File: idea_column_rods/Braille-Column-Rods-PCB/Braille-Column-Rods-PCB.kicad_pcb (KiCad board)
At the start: 2 copper layers, 76 x 95 mm, 64 parts, among them J1 Conn_01x06, J10 Screw_Terminal_01x02, J2 Conn_01x06, J3 Conn_01x06, J4 Conn_01x06, J9 Conn_01x02, M1 Stepper_Motor_bipolar, M2 Stepper_Motor_bipolar, M3 Stepper_Motor_bipolar, M4 Stepper_Motor_bipolar, SW1 SW_Push, SW2 SW_Push, U1 DRV8847SPWR, U2 DRV8847SPWR, U3 DRV8847SPWR, U4 DRV8847SPWR, U9 RP2040-Zero

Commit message: WIP: Rods PCB placement
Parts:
- removed H10, H11, H12, H9: MountingHole_Pad, 00-lib-footprints:MountingHole_2.2mm_M2_Pad_NoSilk
- removed H13, H14, H15, H16: MountingHole_Pad, 00-lib-footprints:MountingHole_3.2mm_M3_Pad_NoSilk
- removed H17, H18, H19, H20: MountingHole_Pad, 00-lib-footprints:HorizMounting_4x_M2_and_M3_Middle
- removed J10: Screw_Terminal_01x02, TerminalBlock:TerminalBlock_bornier-2_P5.08mm
- removed J9: Conn_01x02, Connector_PinHeader_2.54mm:PinHeader_1x02_P2.54mm_Vertical
- added C10: 10u, Capacitor_SMD:C_1206_3216Metric_Pad1.33x1.80mm_HandSolder, F.Cu at (129.5, 103.2)
- added C11: 10u, Capacitor_SMD:C_1206_3216Metric_Pad1.33x1.80mm_HandSolder, F.Cu at (170.1, 87.3)
- added C12: 10u, Capacitor_SMD:C_1206_3216Metric_Pad1.33x1.80mm_HandSolder, F.Cu at (301.4, 72.7)
- added C13: 10u, Capacitor_SMD:C_1206_3216Metric_Pad1.33x1.80mm_HandSolder, F.Cu at (159.7, 142.3)
- added C14: 100n, Capacitor_SMD:C_0603_1608Metric_Pad1.08x0.95mm_HandSolder, F.Cu at (305.0, 81.8)
- added C15: 100n, Capacitor_SMD:C_0603_1608Metric_Pad1.08x0.95mm_HandSolder, F.Cu at (305.0, 84.3)
- added C17: 100n, Capacitor_SMD:C_0603_1608Metric_Pad1.08x0.95mm_HandSolder, F.Cu at (274.8, 115.4)
- added C18: 100n, Capacitor_SMD:C_0603_1608Metric_Pad1.08x0.95mm_HandSolder, F.Cu at (274.8, 135.7)
- added C19: 100n, Capacitor_SMD:C_0603_1608Metric_Pad1.08x0.95mm_HandSolder, F.Cu at (290.4, 115.4)
- added C20: 100n, Capacitor_SMD:C_0603_1608Metric_Pad1.08x0.95mm_HandSolder, F.Cu at (259.1, 115.4)
- added C21: 100n, Capacitor_SMD:C_0603_1608Metric_Pad1.08x0.95mm_HandSolder, F.Cu at (306.1, 115.4)
- added C22: 100n, Capacitor_SMD:C_0603_1608Metric_Pad1.08x0.95mm_HandSolder, F.Cu at (311.4, 84.3)
- added C23: 100n, Capacitor_SMD:C_0603_1608Metric_Pad1.08x0.95mm_HandSolder, F.Cu at (290.4, 135.7)
- added C24: 100n, Capacitor_SMD:C_0603_1608Metric_Pad1.08x0.95mm_HandSolder, F.Cu at (259.1, 135.7)
- added C25: 4.7n, Capacitor_SMD:C_0603_1608Metric_Pad1.08x0.95mm_HandSolder, F.Cu at (274.8, 118.0)
- added C26: 4.7n, Capacitor_SMD:C_0603_1608Metric_Pad1.08x0.95mm_HandSolder, F.Cu at (274.8, 138.2)
- added C27: 4.7n, Capacitor_SMD:C_0603_1608Metric_Pad1.08x0.95mm_HandSolder, F.Cu at (290.4, 118.0)
- added C28: 4.7n, Capacitor_SMD:C_0603_1608Metric_Pad1.08x0.95mm_HandSolder, F.Cu at (259.1, 118.0)
- added C29: 4.7n, Capacitor_SMD:C_0603_1608Metric_Pad1.08x0.95mm_HandSolder, F.Cu at (306.1, 118.0)
- added C30: 4.7n, Capacitor_SMD:C_0603_1608Metric_Pad1.08x0.95mm_HandSolder, F.Cu at (311.4, 86.9)
- added C31: 4.7n, Capacitor_SMD:C_0603_1608Metric_Pad1.08x0.95mm_HandSolder, F.Cu at (290.4, 138.2)
- added C32: 4.7n, Capacitor_SMD:C_0603_1608Metric_Pad1.08x0.95mm_HandSolder, F.Cu at (259.1, 138.2)
- added C33: 100n, Capacitor_SMD:C_0603_1608Metric_Pad1.08x0.95mm_HandSolder, F.Cu at (93.5, 99.8)
- added C34: 4.7n, Capacitor_SMD:C_0603_1608Metric_Pad1.08x0.95mm_HandSolder, F.Cu at (93.5, 94.2)
- added C35: 100n, Capacitor_SMD:C_0603_1608Metric_Pad1.08x0.95mm_HandSolder, F.Cu at (175.2, 87.7)
- added C36: 4.7n, Capacitor_SMD:C_0603_1608Metric_Pad1.08x0.95mm_HandSolder, F.Cu at (175.2, 85.2)
- added C37: 100n, Capacitor_SMD:C_0603_1608Metric_Pad1.08x0.95mm_HandSolder, F.Cu at (296.2, 72.3)
- added C38: 4.7n, Capacitor_SMD:C_0603_1608Metric_Pad1.08x0.95mm_HandSolder, F.Cu at (296.2, 74.8)
- added C39: 100n, Capacitor_SMD:C_0603_1608Metric_Pad1.08x0.95mm_HandSolder, F.Cu at (164.9, 142.7)
- added C40: 4.7n, Capacitor_SMD:C_0603_1608Metric_Pad1.08x0.95mm_HandSolder, F.Cu at (164.9, 140.2)
- added C43: 100n, Capacitor_SMD:C_0603_1608Metric_Pad1.08x0.95mm_HandSolder, F.Cu at (305.0, 86.9)
- added C5: 100n, Capacitor_SMD:C_0603_1608Metric_Pad1.08x0.95mm_HandSolder, F.Cu at (306.1, 112.9)
- added C6: 100n, Capacitor_SMD:C_0603_1608Metric_Pad1.08x0.95mm_HandSolder, F.Cu at (311.4, 81.8)
- added C7: 100n, Capacitor_SMD:C_0603_1608Metric_Pad1.08x0.95mm_HandSolder, F.Cu at (290.4, 133.2)
- added C8: 100n, Capacitor_SMD:C_0603_1608Metric_Pad1.08x0.95mm_HandSolder, F.Cu at (259.1, 133.2)
- added D10: LED, LED_SMD:LED_0603_1608Metric_Pad1.05x0.95mm_HandSolder, F.Cu at (299.7, 146.9)
- added D11: LED, LED_SMD:LED_0603_1608Metric_Pad1.05x0.95mm_HandSolder, F.Cu at (268.4, 146.9)
- added D12: LED, LED_SMD:LED_0603_1608Metric_Pad1.05x0.95mm_HandSolder, F.Cu at (121.4, 105.2)
- added D13: LED, LED_SMD:LED_0603_1608Metric_Pad1.05x0.95mm_HandSolder, F.Cu at (164.8, 87.7)
- added D14: LED, LED_SMD:LED_0603_1608Metric_Pad1.05x0.95mm_HandSolder, F.Cu at (306.6, 72.3)
- added D15: LED, LED_SMD:LED_0603_1608Metric_Pad1.05x0.95mm_HandSolder, F.Cu at (160.5, 139.3)
- added D17: LED, LED_SMD:LED_0603_1608Metric_Pad1.05x0.95mm_HandSolder, F.Cu at (121.4, 107.0)
- added D18: LED, LED_SMD:LED_0603_1608Metric_Pad1.05x0.95mm_HandSolder, F.Cu at (164.8, 85.1)
- added D19: LED, LED_SMD:LED_0603_1608Metric_Pad1.05x0.95mm_HandSolder, F.Cu at (306.6, 74.9)
- added D20: LED, LED_SMD:LED_0603_1608Metric_Pad1.05x0.95mm_HandSolder, F.Cu at (160.5, 136.7)
- added D5: LED, LED_SMD:LED_0603_1608Metric_Pad1.05x0.95mm_HandSolder, F.Cu at (284.1, 146.9)
- added D6: LED, LED_SMD:LED_0603_1608Metric_Pad1.05x0.95mm_HandSolder, F.Cu at (299.7, 126.6)
- added D7: LED, LED_SMD:LED_0603_1608Metric_Pad1.05x0.95mm_HandSolder, F.Cu at (268.4, 126.6)
- added D8: LED, LED_SMD:LED_0603_1608Metric_Pad1.05x0.95mm_HandSolder, F.Cu at (315.4, 126.6)
- added D9: LED, LED_SMD:LED_0603_1608Metric_Pad1.05x0.95mm_HandSolder, F.Cu at (320.7, 95.5)
- added J5: Screw_Terminal_01x02, TerminalBlock:TerminalBlock_bornier-2_P5.08mm, F.Cu at (307.2, 136.5)
- added J6: Screw_Terminal_01x02, TerminalBlock:TerminalBlock_bornier-2_P5.08mm, F.Cu at (307.2, 145.5)
- added J7: Conn_01x02, Connector_PinHeader_2.54mm:PinHeader_1x02_P2.54mm_Vertical, F.Cu at (317.8, 144.0)
- added M10: Motor_DC_With_MP, 00-lib-footprints:DC_Motor_6mm_OD_with_3_Stage_Gearbox, F.Cu at (161.5, 97.0)
- added M11: Motor_DC_With_MP, 00-lib-footprints:DC_Motor_6mm_OD_with_3_Stage_Gearbox, F.Cu at (101.5, 152.0)
- added M12: Motor_DC_With_MP, 00-lib-footprints:DC_Motor_6mm_OD_with_3_Stage_Gearbox, F.Cu at (161.5, 152.0)
- added M5: Stepper_Motor_bipolar, 00-lib-footprints:MicroStepper_8mm-2mmGear, F.Cu at (313.1, 115.2)
- added M6: Stepper_Motor_bipolar, 00-lib-footprints:MicroStepper_8mm-2mmGear, F.Cu at (318.3, 84.1)
- added M7: Stepper_Motor_bipolar, 00-lib-footprints:MicroStepper_8mm-2mmGear, F.Cu at (297.4, 135.5)
- added M8: Stepper_Motor_bipolar, 00-lib-footprints:MicroStepper_8mm-2mmGear, F.Cu at (266.1, 135.5)
- added M9: Motor_DC_With_MP, 00-lib-footprints:DC_Motor_6mm_OD_with_3_Stage_Gearbox, F.Cu at (101.5, 97.0)
- added R13: 2k1, Resistor_SMD:R_0603_1608Metric_Pad0.98x0.95mm_HandSolder, F.Cu at (290.4, 123.0)
- added R14: 330m, Resistor_SMD:R_0603_1608Metric_Pad0.98x0.95mm_HandSolder, F.Cu at (290.4, 125.5)
- added R15: 330m, Resistor_SMD:R_0603_1608Metric_Pad0.98x0.95mm_HandSolder, F.Cu at (290.4, 128.0)
- added R16: 5k1, Resistor_SMD:R_0603_1608Metric_Pad0.98x0.95mm_HandSolder, F.Cu at (259.1, 120.5)
- added R23: 2k1, Resistor_SMD:R_0603_1608Metric_Pad0.98x0.95mm_HandSolder, F.Cu at (306.1, 123.0)
- added R24: 330m, Resistor_SMD:R_0603_1608Metric_Pad0.98x0.95mm_HandSolder, F.Cu at (306.1, 125.5)
- added R25: 330m, Resistor_SMD:R_0603_1608Metric_Pad0.98x0.95mm_HandSolder, F.Cu at (306.1, 128.0)
- added R26: 5k1, Resistor_SMD:R_0603_1608Metric_Pad0.98x0.95mm_HandSolder, F.Cu at (311.4, 89.4)
- added R31: 2k1, Resistor_SMD:R_0603_1608Metric_Pad0.98x0.95mm_HandSolder, F.Cu at (290.4, 143.2)
- added R32: 330m, Resistor_SMD:R_0603_1608Metric_Pad0.98x0.95mm_HandSolder, F.Cu at (290.4, 145.7)
- added R33: 330m, Resistor_SMD:R_0603_1608Metric_Pad0.98x0.95mm_HandSolder, F.Cu at (290.4, 148.2)
- added R34: 5k1, Resistor_SMD:R_0603_1608Metric_Pad0.98x0.95mm_HandSolder, F.Cu at (259.1, 140.7)
- added R35: 2k1, Resistor_SMD:R_0603_1608Metric_Pad0.98x0.95mm_HandSolder, F.Cu at (259.1, 143.2)
- added R36: 330m, Resistor_SMD:R_0603_1608Metric_Pad0.98x0.95mm_HandSolder, F.Cu at (259.1, 145.7)
- added R37: 330m, Resistor_SMD:R_0603_1608Metric_Pad0.98x0.95mm_HandSolder, F.Cu at (259.1, 148.2)
- added R38: 5k1, Resistor_SMD:R_0603_1608Metric_Pad0.98x0.95mm_HandSolder, F.Cu at (125.2, 105.9)
- added R39: 5k1, Resistor_SMD:R_0603_1608Metric_Pad0.98x0.95mm_HandSolder, F.Cu at (175.2, 82.7)
- added R40: 5k1, Resistor_SMD:R_0603_1608Metric_Pad0.98x0.95mm_HandSolder, F.Cu at (296.2, 77.3)
- added R41: 5k1, Resistor_SMD:R_0603_1608Metric_Pad0.98x0.95mm_HandSolder, F.Cu at (164.9, 137.7)
- added R43: 5k1, Resistor_SMD:R_0603_1608Metric_Pad0.98x0.95mm_HandSolder, F.Cu at (305.0, 89.4)
- added R5: 2k1, Resistor_SMD:R_0603_1608Metric_Pad0.98x0.95mm_HandSolder, F.Cu at (274.8, 123.0)
- added R6: 330m, Resistor_SMD:R_0603_1608Metric_Pad0.98x0.95mm_HandSolder, F.Cu at (274.8, 125.5)
- added R7: 330m, Resistor_SMD:R_0603_1608Metric_Pad0.98x0.95mm_HandSolder, F.Cu at (274.8, 128.0)
- added R8: 5k1, Resistor_SMD:R_0603_1608Metric_Pad0.98x0.95mm_HandSolder, F.Cu at (274.8, 140.7)
- added U10: AD116, Package_TO_SOT_SMD:SOT-23-6, F.Cu at (125.5, 103.0)
- added U11: AD116, Package_TO_SOT_SMD:SOT-23-6, F.Cu at (160.1, 86.6)
- added U12: AD116, Package_TO_SOT_SMD:SOT-23-6, F.Cu at (311.4, 73.5)
- added U13: AD116, Package_TO_SOT_SMD:SOT-23-6, F.Cu at (160.2, 133.0)
- added U14: 74HC595, Package_SO:SOP-16_3.9x9.9mm_P1.27mm, F.Cu at (294.2, 103.5)
- added U15: 74HC595, Package_SO:SOP-16_3.9x9.9mm_P1.27mm, F.Cu at (302.8, 103.5)
- added U17: MT910xET, Package_TO_SOT_SMD:SOT-23, F.Cu at (279.4, 127.7)
- added U18: MT910xET, Package_TO_SOT_SMD:SOT-23, F.Cu at (279.4, 148.0)
- added U19: MT910xET, Package_TO_SOT_SMD:SOT-23, F.Cu at (295.1, 127.7)
- added U20: MT910xET, Package_TO_SOT_SMD:SOT-23, F.Cu at (263.8, 127.7)
- added U21: MT910xET, Package_TO_SOT_SMD:SOT-23, F.Cu at (310.7, 127.7)
- added U22: MT910xET, Package_TO_SOT_SMD:SOT-23, F.Cu at (316.0, 96.6)
- added U23: MT910xET, Package_TO_SOT_SMD:SOT-23, F.Cu at (295.1, 148.0)
- added U24: MT910xET, Package_TO_SOT_SMD:SOT-23, F.Cu at (263.8, 148.0)
- added U25: MT910xET, Package_TO_SOT_SMD:SOT-23, F.Cu at (93.8, 97.0)
- added U26: MT910xET, Package_TO_SOT_SMD:SOT-23, F.Cu at (155.1, 86.6)
- added U27: MT910xET, Package_TO_SOT_SMD:SOT-23, F.Cu at (316.4, 73.5)
- added U28: MT910xET, Package_TO_SOT_SMD:SOT-23, F.Cu at (154.3, 141.6)
- added U30: CD74HC4067M, Package_SO:SOIC-24W_7.5x15.4mm_P1.27mm, F.Cu at (296.4, 89.2)
- added U5: DRV8847SPWR, Package_SO:TSSOP-16_4.4x5mm_P0.65mm, F.Cu at (266.1, 122.0)
- added U6: DRV8847SPWR, Package_SO:TSSOP-16_4.4x5mm_P0.65mm, F.Cu at (313.0, 122.0)
- added U7: DRV8847SPWR, Package_SO:TSSOP-16_4.4x5mm_P0.65mm, F.Cu at (318.3, 90.9)
- added U8: DRV8847SPWR, Package_SO:TSSOP-16_4.4x5mm_P0.65mm, F.Cu at (297.4, 142.3)
- C1, C2, C3, C4: footprint Capacitor_SMD:C_1206_3216Metric_Pad1.33x1.80mm_HandSolder -> Capacitor_SMD:C_0603_1608Metric_Pad1.08x0.95mm_HandSolder; moved to F.Cu
- D1, D2, D3, D4: footprint LED_SMD:LED_1206_3216Metric_Pad1.42x1.75mm_HandSolder -> LED_SMD:LED_0603_1608Metric_Pad1.05x0.95mm_HandSolder
- H1, H2, H3, H4, H5, H6: footprint 00-lib-footprints:MountingHole_8mm_Rect_NoSilk -> 00-lib-footprints:MountingHole_3.2mm_M3_Pad_NoSilk
- H7, H8: footprint 00-lib-footprints:MountingHole_2.2mm_M2_Pad_NoSilk -> 00-lib-footprints:MountingHole_3.2mm_M3_Pad_NoSilk
- J1: value Conn_01x06 -> Conn_01x03; footprint 00-lib-footprints:Braille_Cell_Pogos_Solder_2.5mmIntra_6.6x10mmInter -> Connector_PinHeader_2.54mm:PinHeader_1x03_P2.54mm_Vertical
- J2, J3: value Conn_01x06 -> Conn_01x02; footprint 00-lib-footprints:Braille_Cell_Pogos_Solder_2.5mmIntra_6.6x10mmInter -> Connector_PinHeader_2.54mm:PinHeader_1x02_P2.54mm_Vertical
- J4: value Conn_01x06 -> Conn_01x08; footprint 00-lib-footprints:Braille_Cell_Pogos_Solder_2.5mmIntra_6.6x10mmInter -> 00-lib-footprints:SOICbite_clipProgSmall
- R1, R17, R18, R2, R3, R4: footprint Resistor_SMD:R_1206_3216Metric_Pad1.30x1.75mm_HandSolder -> Resistor_SMD:R_0603_1608Metric_Pad0.98x0.95mm_HandSolder
- R10, R11: value 2k1 -> 330m; footprint Resistor_SMD:R_1206_3216Metric_Pad1.30x1.75mm_HandSolder -> Resistor_SMD:R_0603_1608Metric_Pad0.98x0.95mm_HandSolder; moved to F.Cu
- R12: value 2k1 -> 5k1; footprint Resistor_SMD:R_1206_3216Metric_Pad1.30x1.75mm_HandSolder -> Resistor_SMD:R_0603_1608Metric_Pad0.98x0.95mm_HandSolder; moved to F.Cu
- R19, R27: value 330m -> 2k1; footprint Resistor_SMD:R_1206_3216Metric_Pad1.30x1.75mm_HandSolder -> Resistor_SMD:R_0603_1608Metric_Pad0.98x0.95mm_HandSolder; moved to F.Cu
- R20, R21, R28, R29, R9: footprint Resistor_SMD:R_1206_3216Metric_Pad1.30x1.75mm_HandSolder -> Resistor_SMD:R_0603_1608Metric_Pad0.98x0.95mm_HandSolder; moved to F.Cu
- R22, R30: value 330m -> 5k1; footprint Resistor_SMD:R_1206_3216Metric_Pad1.30x1.75mm_HandSolder -> Resistor_SMD:R_0603_1608Metric_Pad0.98x0.95mm_HandSolder; moved to F.Cu
- SW1, SW2: footprint Button_Switch_THT:SW_PUSH_6mm -> 00-lib-footprints:PushButtonSMD_2.93x3.9
- U3: value DRV8847SPWR -> RP2040-Zero; footprint Package_SO:TSSOP-16_4.4x5mm_P0.65mm -> 00-lib-footprints:RP2040 Zero
- U9: value RP2040-Zero -> DRV8847SPWR; footprint 00-lib-footprints:RP2040 Zero -> Package_SO:TSSOP-16_4.4x5mm_P0.65mm
- moved R27 224.0 mm to (311.4, 91.9), turned to 0 degrees
- moved J1 220.5 mm to (317.8, 134.3)
- moved R28 210.7 mm to (311.4, 94.4), turned to 0 degrees
- moved R29 209.7 mm to (311.4, 96.9), turned to 0 degrees
- moved M3 190.9 mm to (297.4, 115.2)
- moved D1 187.7 mm to (284.1, 126.6)
- moved R22 186.6 mm to (306.1, 120.5), turned to 0 degrees
- moved U1 185.1 mm to (281.7, 122.0)
- moved M1 185.1 mm to (281.8, 115.2)
- moved R2 183.2 mm to (285.2, 103.2)
- moved C3 182.1 mm to (290.4, 112.9), turned to 0 degrees
- moved R3 181.3 mm to (285.2, 105.7)
- moved R1 180.7 mm to (274.8, 120.5)
- moved J3 179.2 mm to (285.6, 93.0)
- moved C1 178.3 mm to (274.8, 112.9), turned to 0 degrees
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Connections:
- C1 pad 1: Vdrive -> VDC
- C2 pad 1: Vdrive -> VDC
- C3 pad 1: Vdrive -> VDC
- C4 pad 1: Vdrive -> VDC
- D1 pad 1: /Braille_Cell/~{FAULT} -> /Motor_Control/Braille_Cell_Column/~{FAULT}
- D2 pad 1: /Braille_Cell1/~{FAULT} -> GND
- D3 pad 1: /Braille_Cell2/~{FAULT} -> GND
- D4 pad 1: /Braille_Cell3/~{FAULT} -> GND
- J1 pad 1: unconnected-(J1-Pin_1-Pad1) -> +5V
- J1 pad 2: unconnected-(J1-Pin_2-Pad2) -> VDC
- J1 pad 3: unconnected-(J1-Pin_3-Pad3) -> +3V3
- J2 pad 1: unconnected-(J2-Pin_1-Pad1) -> Net-(J2-Pin_1)
- J2 pad 2: unconnected-(J2-Pin_2-Pad2) -> Net-(J2-Pin_2)
- J3 pad 1: unconnected-(J3-Pin_1-Pad1) -> /Microcontroller/UART0_TX
- J3 pad 2: unconnected-(J3-Pin_2-Pad2) -> /Microcontroller/UART0_RX
- J4 pad 2: unconnected-(J4-Pin_2-Pad2) -> /Microcontroller/UART0_RX
- J4 pad 3: unconnected-(J4-Pin_3-Pad3) -> /Microcontroller/UART0_TX
- J4 pad 4: unconnected-(J4-Pin_4-Pad4) -> GND
- M3 pad 1: Net-(U3-OUT1) -> Net-(U4-OUT1)
- M3 pad 3: Net-(U3-OUT3) -> Net-(U4-OUT3)
- M3 pad 4: Net-(U3-OUT4) -> Net-(U4-OUT4)
- M4 pad 1: Net-(U4-OUT1) -> Net-(U5-OUT1)
- M4 pad 3: Net-(U4-OUT3) -> Net-(U5-OUT3)
- M4 pad 4: Net-(U4-OUT4) -> Net-(U5-OUT4)
- R1 pad 2: /Braille_Cell/~{FAULT} -> /Motor_Control/Braille_Cell_Column/~{FAULT}
- R10 pad 1: +3V3 -> Net-(U2-ISEN34)
- R10 pad 2: Net-(D2-A) -> GND
- R11 pad 1: +3V3 -> Net-(U2-ISEN12)
- R11 pad 2: Net-(D3-A) -> GND
- R12 pad 2: Net-(D4-A) -> /Motor_Control/Braille_Cell_Column2/~{FAULT}
- R19 pad 1: Net-(U1-ISEN34) -> +3V3
- R19 pad 2: GND -> Net-(D7-A)
- R2 pad 1: +3V3 -> /Microcontroller/GP_LED_0
- R2 pad 2: /Braille_Cell1/~{FAULT} -> Net-(D2-A)
- R20 pad 1: Net-(U2-ISEN34) -> Net-(U5-ISEN34)
- R21 pad 1: Net-(U3-ISEN34) -> Net-(U5-ISEN12)
- R22 pad 1: Net-(U4-ISEN34) -> +3V3
- R22 pad 2: GND -> /Motor_Control/Braille_Cell_Column4/~{FAULT}
- R27 pad 1: Net-(U1-ISEN12) -> +3V3
- R27 pad 2: GND -> Net-(D9-A)
- R28 pad 1: Net-(U2-ISEN12) -> Net-(U7-ISEN34)
- R29 pad 1: Net-(U3-ISEN12) -> Net-(U7-ISEN12)
- R3 pad 1: +3V3 -> VDC
- R3 pad 2: /Braille_Cell2/~{FAULT} -> Net-(D3-A)
- R30 pad 1: Net-(U4-ISEN12) -> +3V3
- R30 pad 2: GND -> /Motor_Control/Braille_Cell_Column6/~{FAULT}
- R4 pad 1: +3V3 -> /Microcontroller/GP_LED_1
- R4 pad 2: /Braille_Cell3/~{FAULT} -> Net-(D4-A)
- R9 pad 2: Net-(D1-A) -> Net-(D5-A)
- SW1 pad 2: Net-(U9-GP28) -> /Microcontroller/SW_1
- SW2 pad 2: Net-(U9-GP29) -> /Microcontroller/SW_2
- U1 pad 1: /Braille_Cell/~{SLEEP} -> /Motor_Control/Braille_Cell_Column/~{SLEEP}
- U1 pad 10: /Braille_Cell/IN4 -> unconnected-(U1-IN4-Pad10)
- U1 pad 12: Vdrive -> VDC
- U1 pad 15: /Braille_Cell/IN2 -> unconnected-(U1-IN2-Pad15)
- U1 pad 16: /Braille_Cell/IN1 -> unconnected-(U1-IN1-Pad16)
- U1 pad 8: /Braille_Cell/~{FAULT} -> /Motor_Control/Braille_Cell_Column/~{FAULT}
- U1 pad 9: /Braille_Cell/IN3 -> unconnected-(U1-IN3-Pad9)
- U2 pad 1: /Braille_Cell1/~{SLEEP} -> /Motor_Control/Braille_Cell_Column1/~{SLEEP}
- U2 pad 10: /Braille_Cell1/IN4 -> unconnected-(U2-IN4-Pad10)
- U2 pad 12: Vdrive -> VDC
- U2 pad 15: /Braille_Cell1/IN2 -> unconnected-(U2-IN2-Pad15)
- U2 pad 16: /Braille_Cell1/IN1 -> unconnected-(U2-IN1-Pad16)
- U2 pad 8: /Braille_Cell1/~{FAULT} -> /Motor_Control/Braille_Cell_Column1/~{FAULT}
- U2 pad 9: /Braille_Cell1/IN3 -> unconnected-(U2-IN3-Pad9)
- U3 pad 1: /Braille_Cell2/~{SLEEP} -> +5V
- U3 pad 10: /Braille_Cell2/IN4 -> /Microcontroller/UART0_TX
- U3 pad 11: I2C_SCL -> /Microcontroller/UART0_RX
- U3 pad 12: Vdrive -> /Microcontroller/SHIFT_SER_IN
- U3 pad 13: GND -> /Microcontroller/SHIFT_SRCK
- U3 pad 14: I2C_SDA -> /Microcontroller/~{SHIFT_SRCLR}
- U3 pad 15: /Braille_Cell2/IN2 -> /Microcontroller/SHIFT_RCLK
- U3 pad 16: /Braille_Cell2/IN1 -> /Microcontroller/~{SHIFT_OE}
- U3 pad 2: Net-(U3-OUT1) -> GND
- U3 pad 3: Net-(U3-ISEN12) -> +3V3
- U3 pad 4: Net-(M3--) -> unconnected-(U3-GP29-Pad4)
- U3 pad 5: Net-(U3-OUT4) -> /Microcontroller/SW_1
- U3 pad 6: Net-(U3-ISEN34) -> /Microcontroller/SW_2
- U3 pad 7: Net-(U3-OUT3) -> /Microcontroller/HALL_ANALOG
- U3 pad 8: /Braille_Cell2/~{FAULT} -> Net-(J2-Pin_1)
- U3 pad 9: /Braille_Cell2/IN3 -> Net-(J2-Pin_2)
- U4 pad 1: /Braille_Cell3/~{SLEEP} -> /Motor_Control/Braille_Cell_Column2/~{SLEEP}
- U4 pad 10: /Braille_Cell3/IN4 -> unconnected-(U4-IN4-Pad10)
- U4 pad 12: Vdrive -> VDC
- U4 pad 15: /Braille_Cell3/IN2 -> unconnected-(U4-IN2-Pad15)
- U4 pad 16: /Braille_Cell3/IN1 -> unconnected-(U4-IN1-Pad16)
- U4 pad 4: Net-(M4--) -> Net-(M3--)
- U4 pad 8: /Braille_Cell3/~{FAULT} -> /Motor_Control/Braille_Cell_Column2/~{FAULT}
- U4 pad 9: /Braille_Cell3/IN3 -> unconnected-(U4-IN3-Pad9)
- U9 pad 1: +5V -> /Motor_Control/Braille_Cell_Column7/~{SLEEP}
- U9 pad 10: /Braille_Cell/~{FAULT} -> unconnected-(U9-IN4-Pad10)
- U9 pad 11: /Braille_Cell1/~{FAULT} -> I2C_SCL
- U9 pad 12: /Braille_Cell2/~{FAULT} -> VDC
- U9 pad 13: /Braille_Cell3/~{FAULT} -> GND
- U9 pad 14: /Braille_Cell/IN1 -> I2C_SDA
- U9 pad 15: /Braille_Cell/IN2 -> unconnected-(U9-IN2-Pad15)
- U9 pad 16: /Braille_Cell/IN3 -> unconnected-(U9-IN1-Pad16)
- U9 pad 2: GND -> Net-(U9-OUT1)
- U9 pad 3: +3V3 -> Net-(U9-ISEN12)
- U9 pad 4: Net-(U9-GP29) -> Net-(M8--)
- U9 pad 5: Net-(U9-GP28) -> Net-(U9-OUT4)
- U9 pad 6: I2C_SCL -> Net-(U9-ISEN34)
- U9 pad 7: I2C_SDA -> Net-(U9-OUT3)
- U9 pad 8: unconnected-(U9-GP15-Pad8)_1 -> /Motor_Control/Braille_Cell_Column7/~{FAULT}
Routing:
- net GND: track 192.0 -> 0.00 mm, vias 39 -> 0
- net Vdrive: track 166.6 -> 0.00 mm, vias 2 -> 0
- net I2C_SDA: track 150.7 -> 0.00 mm
- net I2C_SCL: track 148.8 -> 0.00 mm
- net +3V3: track 127.6 -> 1.91 mm, vias 3 -> 0
- net /Braille_Cell/~{FAULT}: track 83.4 -> 0.00 mm
- net /Braille_Cell1/~{FAULT}: track 61.6 -> 0.00 mm
- net /Braille_Cell2/~{FAULT}: track 58.1 -> 0.00 mm, vias 1 -> 0
- net /Braille_Cell2/~{SLEEP}: track 57.9 -> 0.00 mm, vias 1 -> 0
- net /Braille_Cell/IN1: track 51.7 -> 0.00 mm, vias 1 -> 0
- net /Braille_Cell/IN3: track 50.5 -> 0.00 mm, vias 1 -> 0
- net /Braille_Cell/IN2: track 50.4 -> 0.00 mm, vias 1 -> 0
- net /Braille_Cell/~{SLEEP}: track 48.4 -> 0.00 mm, vias 1 -> 0
- net /Braille_Cell/IN4: track 46.0 -> 0.00 mm, vias 1 -> 0
- net /Braille_Cell3/~{FAULT}: track 41.9 -> 0.00 mm, vias 1 -> 0
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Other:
- board size 76 x 95 mm -> 95 x 95 mm
- board text removed: "6.6mm Inter-Cell 2.5mm Intra-Cell M2, M3, and 8mm"
- board text removed: "Braille Display (Pogo + Solenoid) 2024-10-10"
- board text removed: "Vdr GND"
- board text removed: "Vdrive GND"

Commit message: WIP: Place the housing and motor X
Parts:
- removed H3, H4: MountingHole_Pad, 00-lib-footprints:MountingHole_3.2mm_M3_Pad_NoSilk
- H1, H2: footprint 00-lib-footprints:MountingHole_3.2mm_M3_Pad_NoSilk -> 00-lib-footprints:Braille_Block_MountingHoles_M2_3x
- moved U27 236.0 mm to (93.8, 152.1), turned to 180 degrees
- moved C37 218.8 mm to (93.5, 154.8), turned to 180 degrees
- moved C38 215.9 mm to (93.5, 149.2), turned to 180 degrees
- moved M6 209.1 mm to (115.8, 136.0), turned to 90 degrees
- moved U1 205.6 mm to (76.1, 125.3)
- moved U17 205.6 mm to (73.8, 131.0)
- moved C1 205.6 mm to (69.2, 116.2)
- moved C17 205.6 mm to (69.2, 118.7)
- moved C25 205.6 mm to (69.2, 121.2)
- moved R1 205.6 mm to (69.2, 123.7)
- moved R5 205.6 mm to (69.2, 126.2)
- moved R6 205.6 mm to (69.2, 128.7)
- moved R7 205.6 mm to (69.2, 131.2)
- moved D1 205.6 mm to (78.5, 129.9)
- moved D14 205.0 mm to (121.4, 160.2)
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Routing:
- net VDC: track 3.50 -> 14.0 mm
- net Net-(M12--): track 0.00 -> 9.26 mm
- net Net-(M11--): track 0.00 -> 9.26 mm
- net Net-(M10--): track 0.00 -> 9.26 mm
- net Net-(M12-+): track 0.00 -> 6.38 mm
- net Net-(M11-+): track 0.00 -> 6.38 mm
- net Net-(M10-+): track 0.00 -> 6.38 mm
- net +3V3: track 1.91 -> 7.64 mm
- net Net-(D15-A): track 0.00 -> 4.94 mm
- net Net-(D14-A): track 0.00 -> 4.94 mm
- net Net-(D13-A): track 0.00 -> 4.94 mm
- net /Motor_Control/Corner_DC_Motor3/IN_B: track 0.00 -> 4.30 mm
- net /Motor_Control/Corner_DC_Motor2/IN_B: track 0.00 -> 4.30 mm
- net /Motor_Control/Corner_DC_Motor1/IN_B: track 0.00 -> 4.30 mm
- net /Motor_Control/Corner_DC_Motor1/IN_A: track 0.00 -> 2.11 mm
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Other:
- board text added: "Cell Housing: * Mounting hole spacing (X) = 30.5mm * Center = (110.25mm, 125mm)"

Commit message: WIP: Position everything
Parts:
- C17, C25: moved to B.Cu
- M1, M2, M3, M4, M5, M6, M7, M8: footprint 00-lib-footprints:MicroStepper_8mm-2mmGear -> 00-lib-footprints:MicroStepper_4.7_OD
- moved C17 30.6 mm to (99.8, 116.4), turned to -90 degrees
- moved C25 28.9 mm to (97.8, 116.4), turned to -90 degrees
- moved U17 28.9 mm to (98.8, 116.3), turned to -90 degrees
- moved D20 5.03 mm to (141.8, 147.0)
- moved C10 5.00 mm to (129.5, 98.2)
- moved C11 5.00 mm to (133.5, 85.8)
- moved C12 5.00 mm to (129.5, 163.2)
- moved C13 5.00 mm to (133.5, 150.8)
- moved C33 5.00 mm to (93.5, 94.8)
- moved C34 5.00 mm to (93.5, 89.2)
- moved C35 5.00 mm to (169.5, 89.2)
- moved C36 5.00 mm to (169.5, 94.7)
- moved C37 5.00 mm to (93.5, 159.8)
- moved C38 5.00 mm to (93.5, 154.2)
- moved C39 5.00 mm to (169.5, 154.2)
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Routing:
- net /Motor_Control/Corner_DC_Motor/IN_B: track 4.30 -> 6.14 mm
- net /Motor_Control/HALL_0: vias 0 -> 1
- net +3V3: vias 0 -> 1

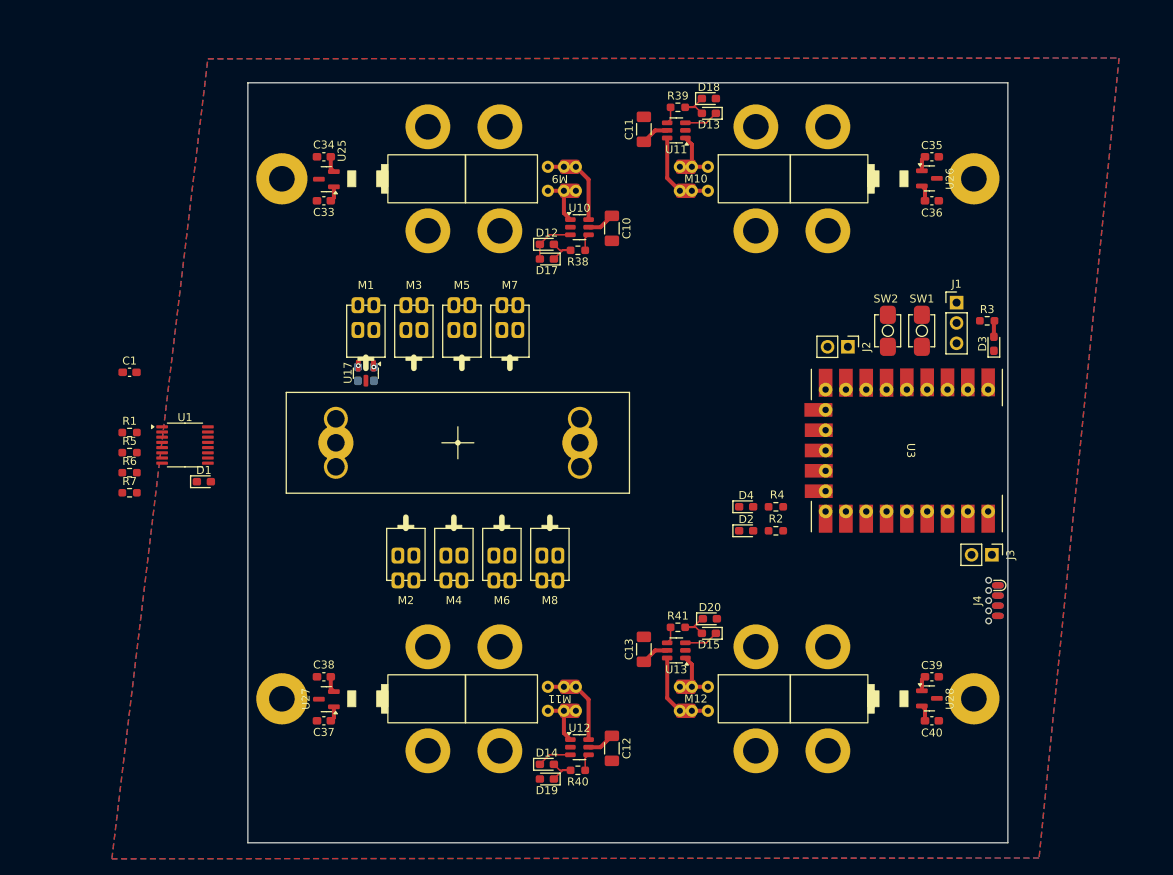
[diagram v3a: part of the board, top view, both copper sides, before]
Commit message: WIP: Update tight placement of DC motor
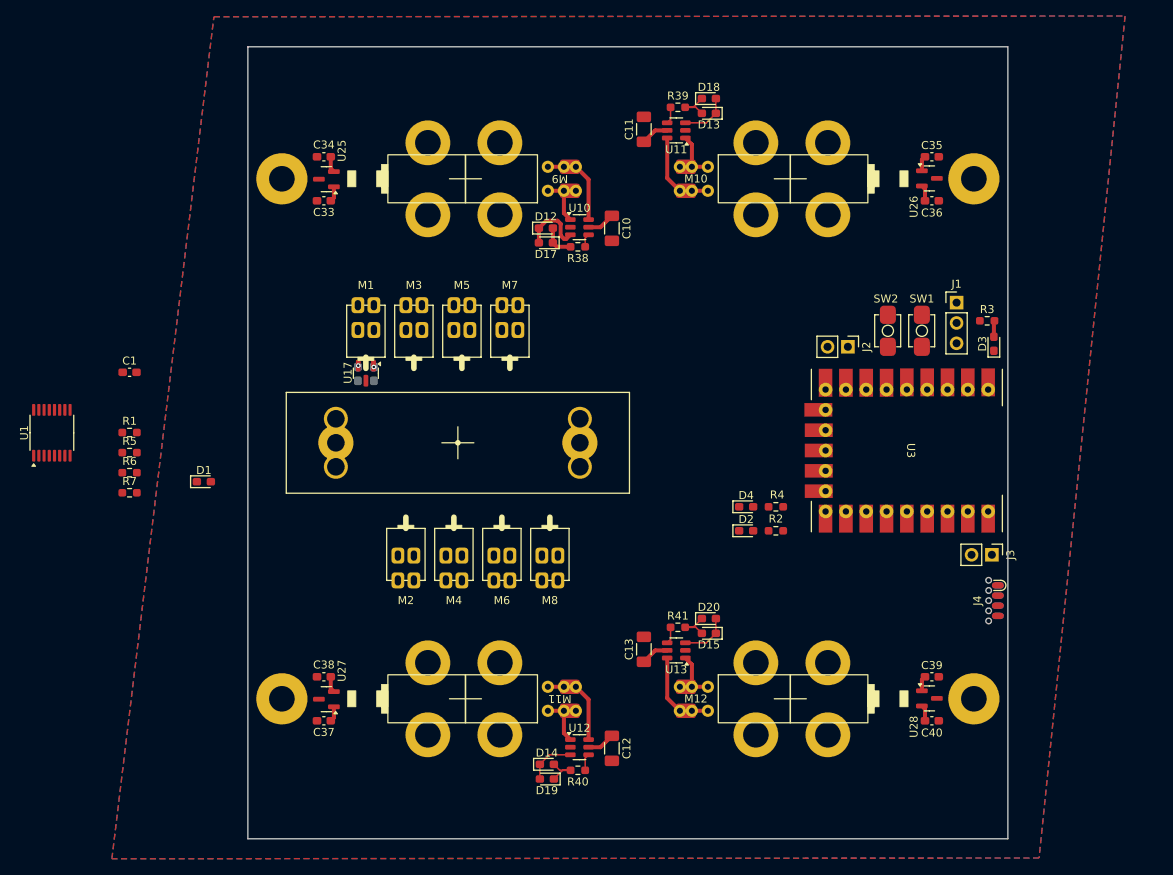
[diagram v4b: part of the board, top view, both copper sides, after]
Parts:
- moved U1 16.7 mm to (59.5, 123.8), turned to 90 degrees
- moved D12 2.03 mm to (121.2, 98.2)
- moved D17 2.03 mm to (121.2, 100.0)
- moved R38 0.44 mm to (125.2, 100.5)
- moved D20 0.13 mm to (141.6, 147.0)
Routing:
- net /Motor_Control/Corner_DC_Motor/IN_B: track 6.14 -> 8.17 mm
- net /Motor_Control/Corner_DC_Motor3/IN_B: track 4.30 -> 6.14 mm
- net /Motor_Control/Corner_DC_Motor2/IN_B: track 4.30 -> 6.14 mm
- net /Motor_Control/Corner_DC_Motor1/IN_B: track 4.30 -> 6.14 mm
- net Net-(D12-A): track 4.94 -> 4.26 mm
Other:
- board size 95 x 95 mm -> 95 x 99 mm

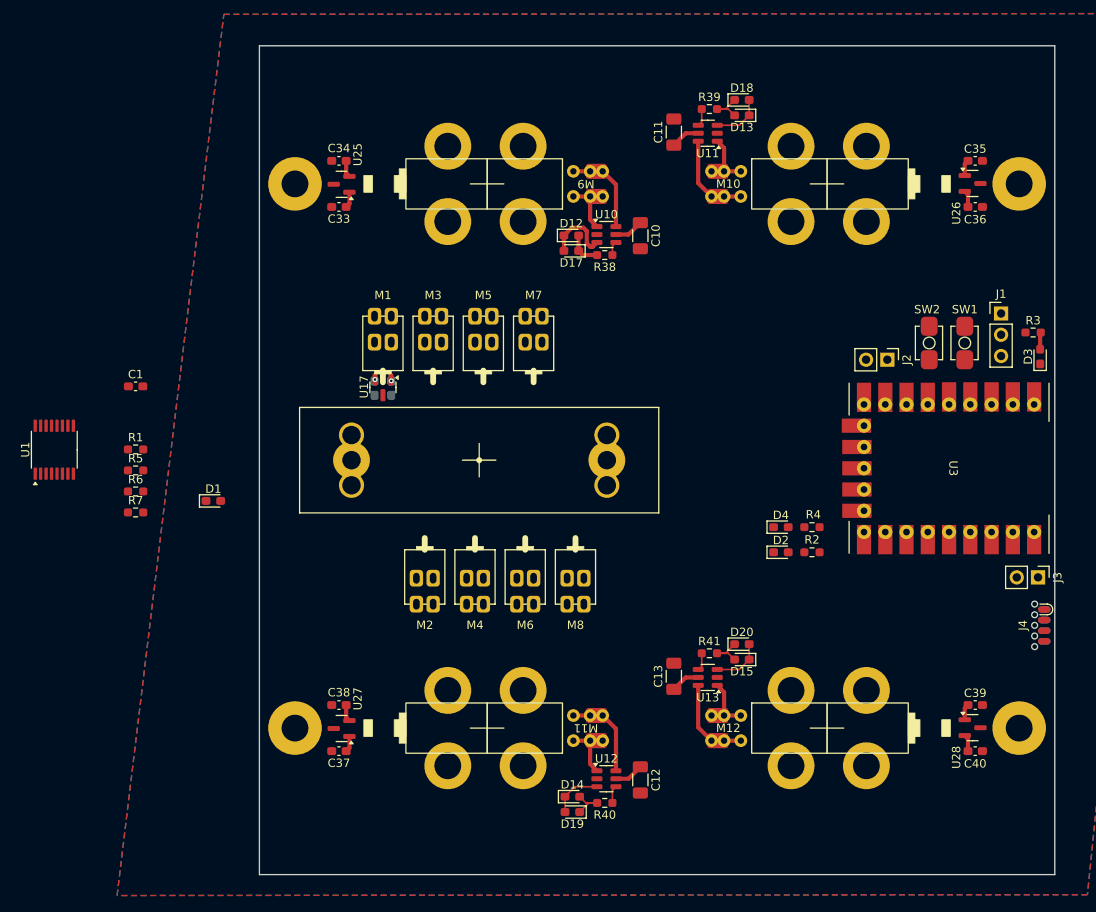
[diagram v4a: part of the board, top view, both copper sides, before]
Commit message: WIP: Layout and route the stepper driver
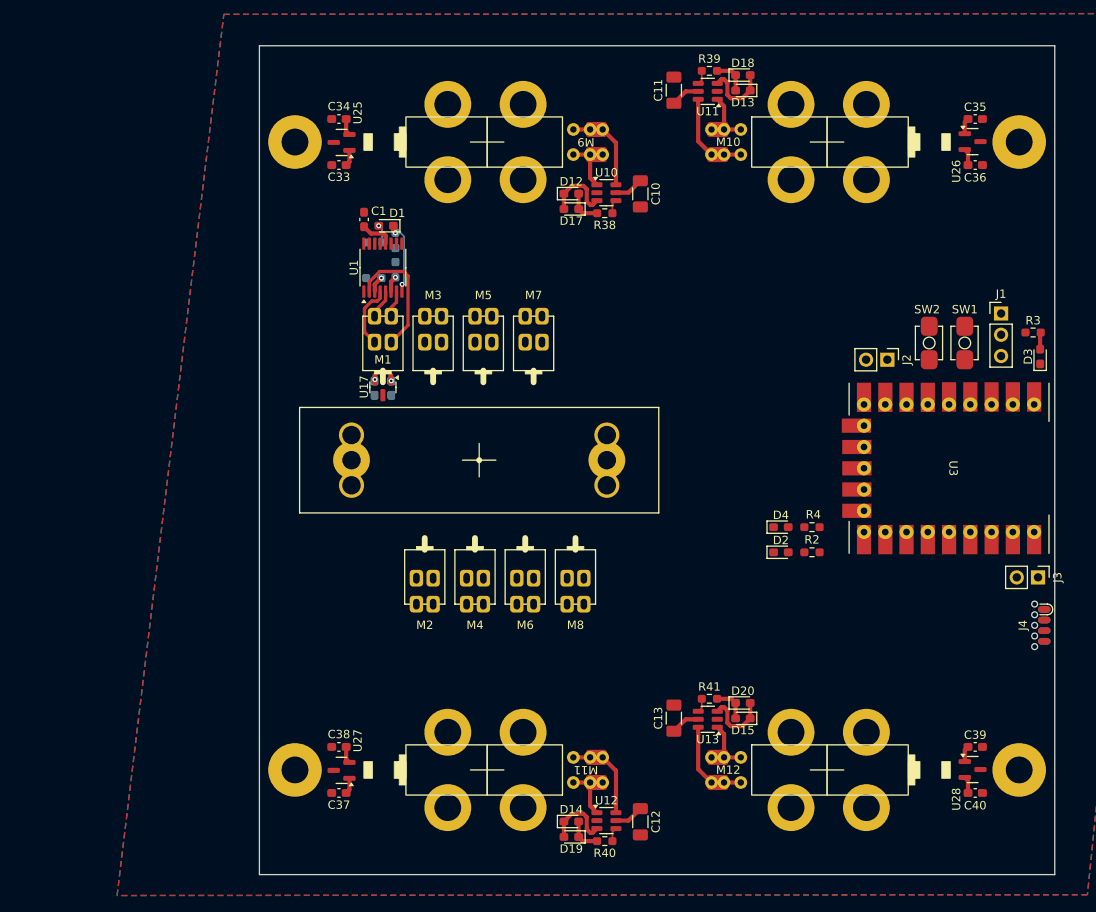
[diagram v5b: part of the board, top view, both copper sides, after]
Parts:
- R1, R5, R6, R7: moved to B.Cu
- moved U1 44.9 mm to (98.8, 102.0)
- moved R6 40.8 mm to (100.2, 102.2), turned to 90 degrees
- moved R7 39.9 mm to (97.7, 103.2), turned to 180 degrees
- moved R1 39.8 mm to (100.2, 98.8), turned to 90 degrees
- moved R5 39.4 mm to (97.8, 99.0)
- moved D1 38.8 mm to (99.1, 97.0), turned to 180 degrees
- moved C1 33.8 mm to (96.5, 96.2), turned to 90 degrees
- moved D15 7.03 mm to (141.8, 155.8)
- moved D20 7.03 mm to (141.8, 154.0)
- moved R41 5.44 mm to (137.8, 153.5)
- moved C10 5.00 mm to (129.5, 93.2)
- moved C11 5.00 mm to (133.5, 80.8)
- moved C12 5.00 mm to (129.5, 168.2)
- moved C13 5.00 mm to (133.5, 155.8)
- moved C33 5.00 mm to (93.5, 89.8)
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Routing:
- net Net-(U1-OUT1): track 0.00 -> 15.2 mm
- net /Motor_Control/Braille_Cell_Column/~{FAULT}: track 0.00 -> 8.82 mm, vias 0 -> 2
- net Net-(M1--): track 0.00 -> 7.70 mm
- net VDC: track 14.0 -> 18.0 mm
- net Net-(U1-OUT4): track 0.00 -> 3.49 mm
- net Net-(U1-OUT3): track 0.00 -> 3.20 mm
- net Net-(D1-A): track 0.00 -> 2.17 mm, vias 0 -> 1
- net /Motor_Control/Corner_DC_Motor1/IN_B: track 6.14 -> 8.17 mm
- net /Motor_Control/Corner_DC_Motor2/IN_B: track 6.14 -> 8.17 mm
- net /Motor_Control/Corner_DC_Motor3/IN_B: track 6.14 -> 8.17 mm
- net Net-(U1-ISEN12): track 0.00 -> 1.98 mm, vias 0 -> 1
- net Net-(U1-ISEN34): track 0.00 -> 1.92 mm, vias 0 -> 1
- net Net-(D15-A): track 4.94 -> 4.26 mm
- net Net-(D14-A): track 4.94 -> 4.26 mm
- net Net-(D13-A): track 4.94 -> 4.26 mm

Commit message: WIP: Motor layout is good
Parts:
- C18, C19, C20, C21, C22, C23, C24, C26, C27, C28, C29, C30, C31, C32, R10, R11, R12, R13, R14, R15, R16, R19, R20, R21, R22, R23, R24, R25, R26, R27, R28, R29, R30, R31, R32, R33, R34, R35, R36, R37, R8, R9: moved to B.Cu
- moved D9 213.2 mm to (115.4, 153.0)
- moved U7 210.5 mm to (115.8, 148.0), turned to -90 degrees
- moved R26 206.6 mm to (114.3, 151.2), turned to -90 degrees
- moved D8 206.4 mm to (111.1, 97.0), turned to 180 degrees
- moved C6 206.3 mm to (118.0, 153.8), turned to -90 degrees
- moved R28 204.2 mm to (114.3, 147.8), turned to -90 degrees
- moved U22 203.7 mm to (115.8, 133.7), turned to 90 degrees
- moved R27 203.4 mm to (116.8, 151.0), turned to 180 degrees
- moved U6 203.3 mm to (110.8, 102.0), turned to 90 degrees
- moved C22 202.7 mm to (114.8, 133.6), turned to 90 degrees
- moved R29 200.8 mm to (116.8, 146.8)
- moved U21 200.3 mm to (110.8, 116.3), turned to -90 degrees
- moved C30 200.2 mm to (116.7, 133.6), turned to 90 degrees
- moved C5 198.3 mm to (108.5, 96.2), turned to 90 degrees
- moved R25 198.0 mm to (109.7, 103.2), turned to 180 degrees
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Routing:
- net VDC: track 18.0 -> 42.0 mm
- net Net-(U9-OUT1): track 0.00 -> 15.2 mm
- net Net-(U7-OUT1): track 0.00 -> 15.2 mm
- net Net-(U5-OUT1): track 0.00 -> 15.2 mm
- net Net-(U2-OUT1): track 0.00 -> 15.2 mm
- net Net-(U8-OUT1): track 0.00 -> 15.2 mm
- net Net-(U4-OUT1): track 0.00 -> 15.2 mm
- net Net-(U6-OUT1): track 0.00 -> 15.2 mm
- net /Motor_Control/Braille_Cell_Column7/~{FAULT}: track 0.00 -> 8.82 mm, vias 0 -> 2
- net /Motor_Control/Braille_Cell_Column5/~{FAULT}: track 0.00 -> 8.82 mm, vias 0 -> 2
- net /Motor_Control/Braille_Cell_Column3/~{FAULT}: track 0.00 -> 8.82 mm, vias 0 -> 2
- net /Motor_Control/Braille_Cell_Column1/~{FAULT}: track 0.00 -> 8.82 mm, vias 0 -> 2
- net /Motor_Control/Braille_Cell_Column6/~{FAULT}: track 0.00 -> 8.82 mm, vias 0 -> 2
- net /Motor_Control/Braille_Cell_Column4/~{FAULT}: track 0.00 -> 8.82 mm, vias 0 -> 2
- net /Motor_Control/Braille_Cell_Column2/~{FAULT}: track 0.00 -> 8.82 mm, vias 0 -> 2
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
